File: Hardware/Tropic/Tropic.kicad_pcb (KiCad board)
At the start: 4 copper layers, 35.8 x 24.7 mm, 34 parts, among them J1 0734120114, J2 68610414422, J4 53309-1070, Q3 FDN340P, SW1 B3U-3000P, U1 ESP32-PICO-D4, U4 NCP1117ST33T3G

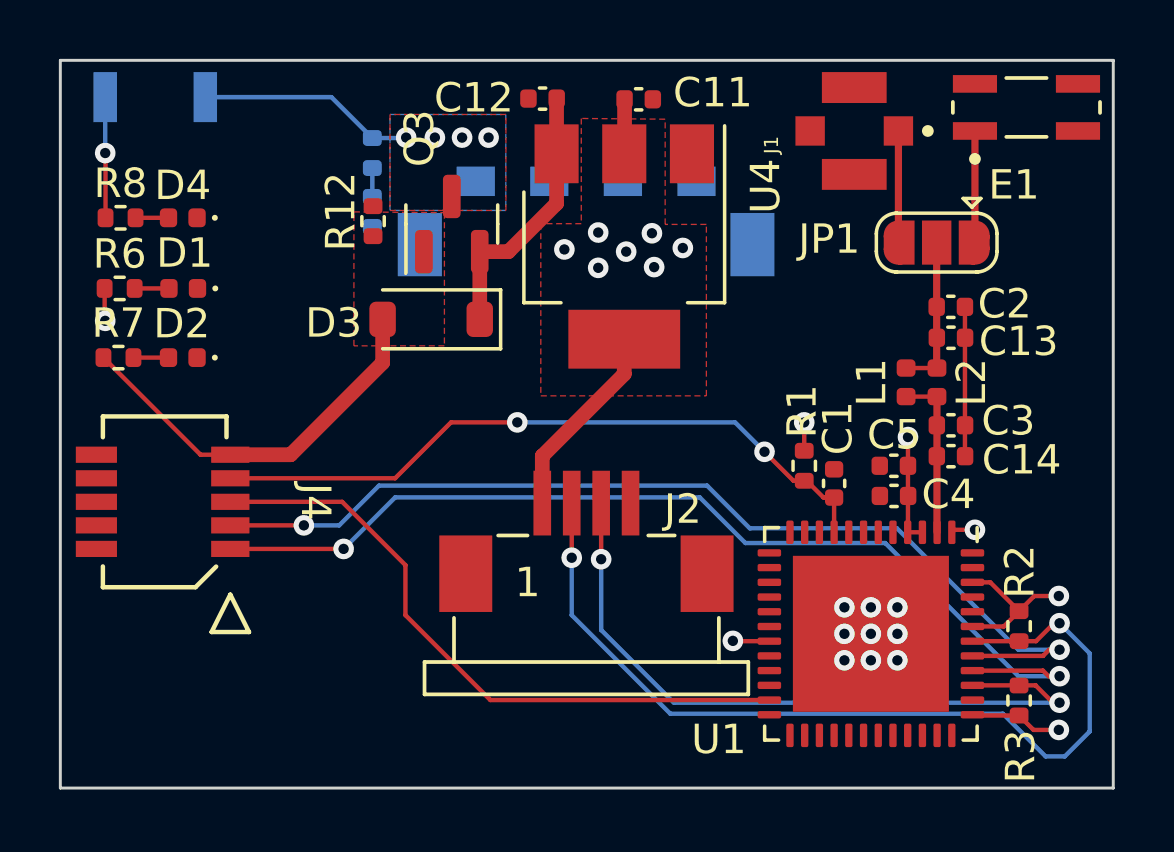
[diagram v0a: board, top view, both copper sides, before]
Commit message: Removed doubled Pi Matching and add LED for voltage monitoring
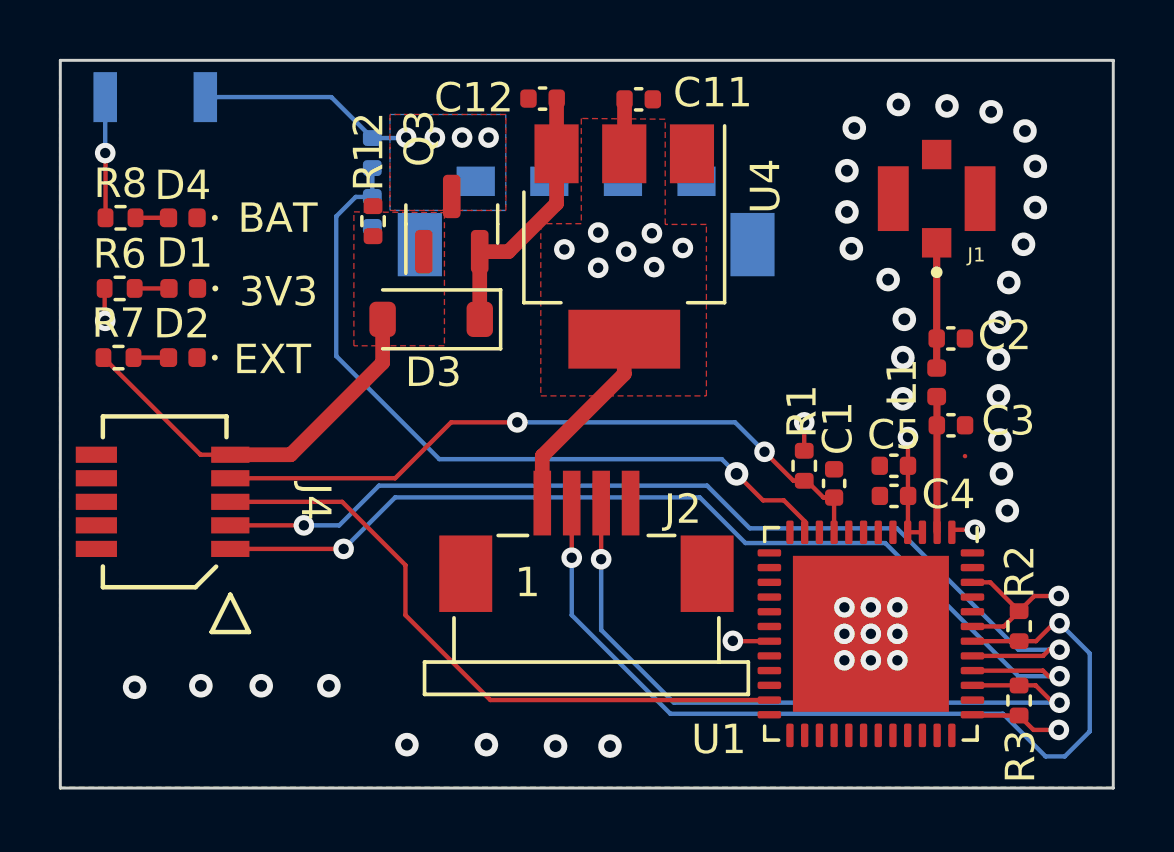
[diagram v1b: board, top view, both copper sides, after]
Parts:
- removed C13, C14: TBD, Capacitor_SMD:C_0402_1005Metric
- removed E1: 2450AT42E010BE, manul_tech:XDCR_2450AT42E010BE
- removed JP1: Antenna Selector, Jumper:SolderJumper-3_P1.3mm_Open_RoundedPad1.0x1.5mm
- removed L2: TBD, Inductor_SMD:L_0402_1005Metric
- moved J1 3.62 mm to (208.2, 19.9), turned to 0 degrees
- moved C2 1.07 mm to (208.7, 24.7)
- moved L1 1.04 mm to (208.2, 26.2)
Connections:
- C2 pad 1: Net-(JP1-C) -> Net-(C2-Pad1)
- J1 pad 1: Net-(JP1-B) -> Net-(C2-Pad1)
- L1 pad 2: Net-(JP1-C) -> Net-(C2-Pad1)
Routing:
- net /MCU/GPI35: track 0.98 -> 25.8 mm, vias 0 -> 1
- net Net-(JP1-C): track 5.32 -> 0.00 mm
- net GND: track 5.08 -> 0.01 mm, vias 9 -> 39
- net Net-(C2-Pad1): track 0.00 -> 4.27 mm
- net Net-(JP1-B): track 3.79 -> 0.00 mm
- net Net-(JP1-A): track 3.79 -> 0.00 mm
- net Net-(U1-LNA_IN): track 5.66 -> 4.61 mm
- added copper zone on In1.Cu, net +3.3V
- added copper zone on B.Cu, net GND
- added copper zone on F.Cu, net GND
- added copper zone on In2.Cu, net GND
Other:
- board text added: "3V3"
- board text added: "BAT"
- board text added: "EXT"

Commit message: Completed design V1
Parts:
- added D5: 1N5819W, Diode_SMD:D_SOD-123, F.Cu at (191.2, 20.5)
- moved R2 16.6 mm to (195.8, 27.9)
- moved R3 7.63 mm to (203.4, 35.9), turned to -90 degrees
- moved C4 5.70 mm to (209.1, 24.8)
- moved C1 5.70 mm to (207.0, 24.4)
- moved C5 5.70 mm to (209.1, 23.8)
- moved R1 5.70 mm to (206.0, 23.8)
- moved U1 5.70 mm to (208.3, 29.5)
- moved D3 4.19 mm to (190.4, 28.2)
- moved R12 4.19 mm to (188.5, 24.9)
- moved Q3 4.19 mm to (191.2, 25.0)
- moved C2 3.64 mm to (211.0, 21.9)
- moved C3 3.64 mm to (211.0, 24.8)
- moved L1 3.64 mm to (210.5, 23.4)
- moved J1 2.64 mm to (210.5, 18.6)
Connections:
- BATT1 pad 1: +BATT -> Net-(BATT1-B+)
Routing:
- net +BATT: track 7.42 -> 15.5 mm, vias 4 -> 1
- net /MCU/SDA: track 31.0 -> 23.5 mm
- net GND: track 0.01 -> 3.95 mm, vias 39 -> 28
- net Net-(D3-K): track 9.17 -> 13.0 mm
- net /MCU/EN: track 23.5 -> 26.9 mm
- net VDC: track 13.6 -> 10.5 mm
- net /MCU/GPI35: track 25.8 -> 28.7 mm
- net Net-(U1-LNA_IN): track 4.61 -> 2.22 mm
- net Net-(C2-Pad1): track 4.27 -> 2.76 mm
- net /MCU/RX: track 34.5 -> 33.2 mm
- net /MCU/IO0: track 22.1 -> 23.3 mm, vias 0 -> 2
- net /MCU/TX: track 34.1 -> 33.4 mm
- net /MCU/SCL: track 24.1 -> 24.4 mm, vias 2 -> 0
- net Net-(BATT1-B+): track 0.00 -> 0.01 mm, vias 0 -> 4
- added copper zone on B.Cu, net Net-(BATT1-B+)
- added copper zone on F.Cu, net Net-(BATT1-B+)
- removed copper zone on B.Cu, net +BATT
- removed copper zone on F.Cu, net +BATT
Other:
- board text added: "M-Sens Tropic by Manul Technologies"
